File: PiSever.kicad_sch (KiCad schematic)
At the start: 11 parts, among them J1 USB_C_Receptacle, J2 Fan, J3 BMP, J4 RX Ant, J5 TX Ant, P1 USB_C_Plug, U1 QFM-RX1-433, U2 AK-FST

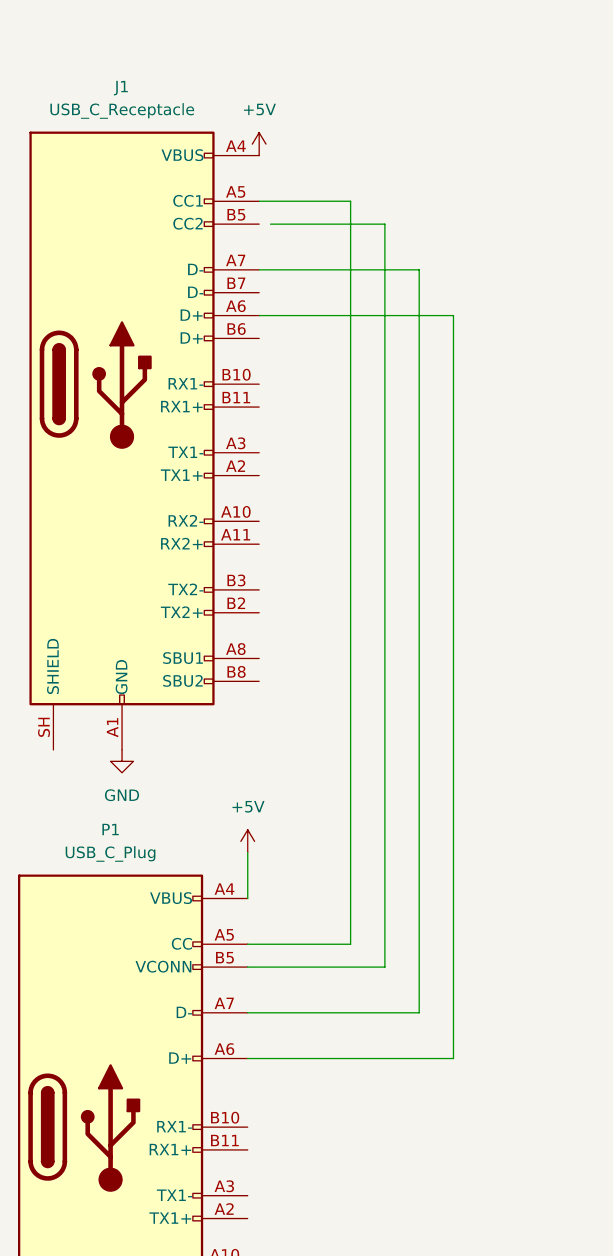
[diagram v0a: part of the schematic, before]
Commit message: Add through hole usb
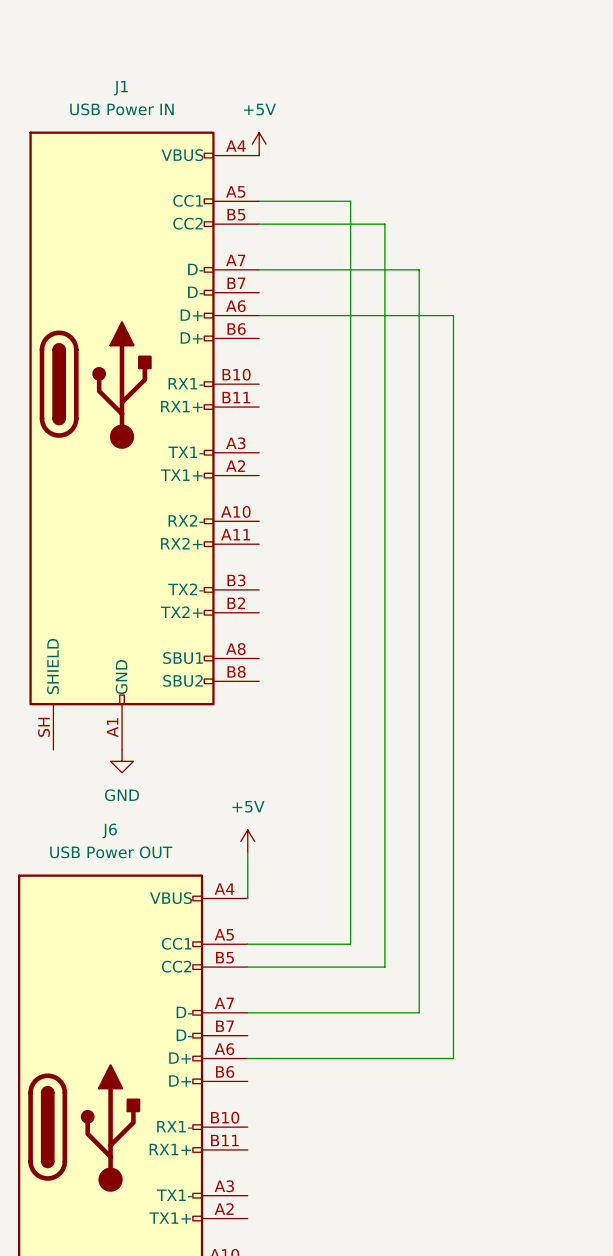
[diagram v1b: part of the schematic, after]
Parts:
- removed P1: USB_C_Plug, Connector_USB:USB_C_Plug_Molex_105444, symbol Connector:USB_C_Plug
- added J6: USB Power OUT, Connector_USB:USB_C_Receptacle_GCT_USB4085, symbol Connector:USB_C_Receptacle
- J1: value USB_C_Receptacle -> USB Power IN; footprint Connector_USB:USB_C_Receptacle_HRO_TYPE-C-31-M-17 -> Connector_USB:USB_C_Receptacle_GCT_USB4085
- J4, J5: footprint Connector_PinHeader_2.54mm:PinHeader_1x01_P2.54mm_Horizontal -> Connector_PinHeader_2.54mm:PinHeader_1x01_P2.54mm_Vertical
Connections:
- net +5V: now also J6.A4 (VBUS), J6.A9 (VBUS), J6.B4 (VBUS), J6.B9 (VBUS)
- net GND: now also J6.A1 (GND), J6.A12 (GND), J6.B1 (GND), J6.B12 (GND)
- net at J1.A5 (CC1): now also J6.A5 (CC1)
- net at J1.A6 (D+): now also J6.A6 (D+)
- net at J1.A7 (D-): now also J6.A7 (D-)
- net at J1.B5 (CC2): now also J6.B5 (CC2)
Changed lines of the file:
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@@
 	(wire
 		(pts
-			(xy 74.93 43.18) (xy 87.63 43.18)
+			(xy 147.32 93.98) (xy 189.23 93.98)
 		)
 		(stroke
@@
 	(wire
 		(pts
-			(xy 147.32 93.98) (xy 189.23 93.98)
+			(xy 87.63 125.73) (xy 72.39 125.73)
 		)
 		(stroke
@@
 	(wire
 		(pts
-			(xy 87.63 125.73) (xy 72.39 125.73)
+			(xy 73.66 43.18) (xy 87.63 43.18)
 		)
 		(stroke
@@
 			)
 		)
-		(property "Value" "USB_C_Receptacle"
+		(property "Value" "USB Power IN"
 			(at 58.42 30.48 0)
 			(show_name no)
@@
 			)
 		)
-		(property "Footprint" "Connector_USB:USB_C_Receptacle_HRO_TYPE-C-31-M-17"
+		(property "Footprint" "Connector_USB:USB_C_Receptacle_GCT_USB4085"
 			(at 62.23 60.96 0)
 			(hide yes)
@@
 	)
 	(symbol
-		(lib_id "Connector:USB_C_Plug")
-		(at 57.15 143.51 0)
-		(unit 1)
-		(body_style 1)
-		(exclude_from_sim no)
-		(in_bom yes)
-		(on_board yes)
-		(in_pos_files yes)
-		(dnp no)
-		(fields_autoplaced yes)
-		(property "Reference" "P1"
-			(at 57.15 110.49 0)
-			(show_name no)
-			(do_not_autoplace no)
-			(effects
-				(font
-					(size 1.27 1.27)
-				)
-			)
-		)
-		(property "Value" "USB_C_Plug"
-			(at 57.15 113.03 0)
-			(show_name no)
-			(do_not_autoplace no)
-			(effects
-				(font
-					(size 1.27 1.27)
-				)
-			)
-		)
-		(property "Footprint" "Connector_USB:USB_C_Plug_Molex_105444"
-			(at 60.96 143.51 0)
-			(hide yes)
-			(show_name no)
-			(do_not_autoplace no)
-			(effects
-				(font
-					(size 1.27 1.27)
-				)
-			)
-		)
-		(property "Datasheet" "https://www.usb.org/sites/default/files/documents/usb_type-c.zip"
-			(at 60.96 143.51 0)
-			(hide yes)
-			(show_name no)
-			(do_not_autoplace no)
-			(effects
-				(font
-					(size 1.27 1.27)
-				)
-			)
-		)
-		(property "Description" "USB Type-C Plug connector"
-			(at 57.15 143.51 0)
-			(hide yes)
-			(show_name no)
-			(do_not_autoplace no)
-			(effects
-				(font
-					(size 1.27 1.27)
-				)
-			)
-		)
-		(pin "B5"
-		)
-		(pin "A9"
-		)
-		(pin "B12"
-		)
-		(pin "A6"
-		)
-		(pin "SH"
-		)
-		(pin "A12"
-		)
-		(pin "A1"
-		)
-		(pin "A4"
-		)
-		(pin "A8"
-		)
-		(pin "B3"
-		)
-		(pin "B4"
-		)
-		(pin "B9"
-		)
-		(pin "A10"
-		)
-		(pin "B11"
-		)
-		(pin "A2"
-		)
-		(pin "A11"
-		)
-		(pin "B1"
-		)
-		(pin "B2"
-		)
-		(pin "A5"
-		)
-		(pin "A3"
-		)
-		(pin "A7"
-		)
-		(pin "B8"
-		)
-		(pin "B10"
-		)
-		(instances
-			(project "PiSever"
-				(path "/bccedc26-e990-49ec-a52a-1a019beb02ec"
-					(reference "P1")
-					(unit 1)
-				)
-			)
-		)
-	)
-	(symbol
 		(lib_id "Connector:Conn_01x01_Pin")
 		(at 116.84 153.67 0)
@@
 			)
 		)
-		(property "Footprint" "Connector_PinHeader_2.54mm:PinHeader_1x01_P2.54mm_Horizontal"
+		(property "Footprint" "Connector_PinHeader_2.54mm:PinHeader_1x01_P2.54mm_Vertical"
 			(at 116.84 153.67 0)
 			(hide yes)
@@
 			)
 		)
-		(property "Footprint" "Connector_PinHeader_2.54mm:PinHeader_1x01_P2.54mm_Horizontal"
+		(property "Footprint" "Connector_PinHeader_2.54mm:PinHeader_1x01_P2.54mm_Vertical"
 			(at 198.12 153.67 0)
 			(hide yes)
@@
 					(unit 1)
 				)
+			)
+		)
+	)
+	(symbol
+		(lib_id "Connector:USB_C_Receptacle")
+		(at 57.15 143.51 0)
+		(unit 1)
+		(body_style 1)
+		(exclude_from_sim no)
+		(in_bom yes)
+		(on_board yes)
+		(in_pos_files yes)
+		(dnp no)
+		(fields_autoplaced yes)
+		(property "Reference" "J6"
+			(at 57.15 110.49 0)
+			(show_name no)
+			(do_not_autoplace no)
+			(effects
+				(font
+					(size 1.27 1.27)
+				)
+			)
+		)
+		(property "Value" "USB Power OUT"
+			(at 57.15 113.03 0)
+			(show_name no)
+			(do_not_autoplace no)
+			(effects
+				(font
+					(size 1.27 1.27)
+				)
+			)
+		)
+		(property "Footprint" "Connector_USB:USB_C_Receptacle_GCT_USB4085"
+			(at 60.96 143.51 0)
+			(hide yes)
+			(show_name no)
+			(do_not_autoplace no)
+			(effects
+				(font
+					(size 1.27 1.27)
+				)
+			)
+		)
+		(property "Datasheet" "https://www.usb.org/sites/default/files/documents/usb_type-c.zip"
+			(at 60.96 143.51 0)
+			(hide yes)
+			(show_name no)
+			(do_not_autoplace no)
+			(effects
+				(font
+					(size 1.27 1.27)
+				)
+			)
+		)
+		(property "Description" "USB Full-Featured Type-C Receptacle connector"
+			(at 57.15 143.51 0)
+			(hide yes)
+			(show_name no)
+			(do_not_autoplace no)
+			(effects
+				(font
+					(size 1.27 1.27)
+				)
+			)
+		)
+		(pin "B8"
+		)
+		(pin "B10"
+		)
+		(pin "B12"
+		)
+		(pin "A10"
+		)
+		(pin "A8"
+		)
+		(pin "A9"
+		)
+		(pin "A5"
+		)
+		(pin "A6"
+		)
+		(pin "A2"
+		)
+		(pin "A12"
+		)
+		(pin "B1"
+		)
+		(pin "A3"
+		)
+		(pin "A11"
+		)
+		(pin "A4"
+		)
+		(pin "A1"
+		)
+		(pin "B2"
+		)
+		(pin "B4"
+		)
+		(pin "B5"
+		)
+		(pin "B6"
+		)
+		(pin "A7"
+		)
+		(pin "B3"
+		)
+		(pin "B7"
+		)
+		(pin "B9"
+		)
+		(pin "B11"
+		)
+		(pin "SH"
+		)
+		(instances
+			(project "PiSever"
+				(path "/bccedc26-e990-49ec-a52a-1a019beb02ec"
+					(reference "J6")
+					(unit 1)
+				)

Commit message: Re-route
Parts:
- removed J3: BMP, Connector_PinSocket_2.54mm:PinSocket_1x04_P2.54mm_Vertical, symbol Connector:Conn_01x04_Socket
- removed R1, R2: R4.7k, Resistor_THT:R_Axial_DIN0207_L6.3mm_D2.5mm_P7.62mm_Horizontal, symbol Device:R
- added J3: BMP 280, symbol Connector:Conn_01x04_Pin
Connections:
- net +5V: no longer A1.30 (VIN), U1.4 (SUPPLY_VOLTAGE), U1.5 (SUPPLY_VOLTAGE), U2.4 (SUPPLY_VOLTAGE)
- net GND: now also J3.2 (Pin_2)
- net FAN_TACH: now reaches A1.6 (D3), J2.3 (Pin_3)
- net FAN_PWM: now reaches A1.12 (D9), J2.4 (Pin_4)
- net SDA: now reaches A1.23 (A4)
- net SDA: now also J3.4 (Pin_4)
- net SCL: now reaches A1.24 (A5)
- net SCL: now also J3.3 (Pin_3)
- net at A1.15 (D12): now also U2.3 (DATA_OUTPUT)
- net +5v_Arduino: now reaches A1.27 (+5V)
- net +5v_Arduino: now also U1.4 (SUPPLY_VOLTAGE), U1.5 (SUPPLY_VOLTAGE), U2.4 (SUPPLY_VOLTAGE), J3.1 (Pin_1)
- net at A1.5 (D2): now also U1.7 (DATA_OUTPUT)
- net at A1.7 (D4): no longer U1.7 (DATA_OUTPUT)
- net at A1.8 (D5): no longer U2.3 (DATA_OUTPUT)
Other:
- moved on the sheet: A1, J2, J4, J5, U1, U2
